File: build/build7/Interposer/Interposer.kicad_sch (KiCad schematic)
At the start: 2 parts, among them U1 BQ21040DBVR, U2 BQ21040DBVR

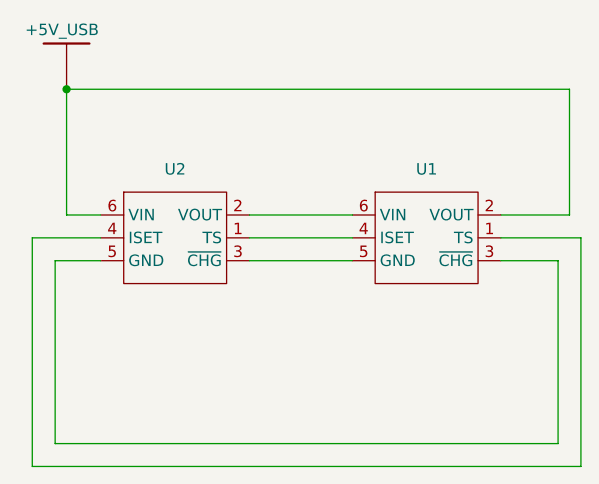
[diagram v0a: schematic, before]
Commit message: Current status: debugged and fixed 4 boards, need to finalize firmware and finish building these 4. All lamps from first build came unglued, need to revise design/assembly to fix this
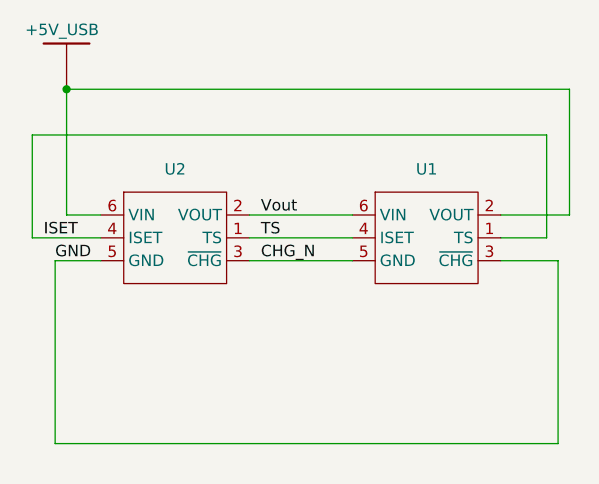
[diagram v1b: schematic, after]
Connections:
- net ISET: now reaches U1.1 (TS), U2.4 (ISET)
- net GND: now reaches U1.3 (~{CHG}), U2.5 (GND)
- net TS: now reaches U1.4 (ISET), U2.1 (TS)
- net CHG_N: now reaches U1.5 (GND), U2.3 (~{CHG})
- net Vout: now reaches U1.6 (VIN), U2.2 (VOUT)
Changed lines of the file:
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@@
-	(wire
-		(pts
-			(xy 161.29 124.46) (xy 161.29 99.06)
-		)
-		(stroke
-			(width 0)
-			(type default)
-		)
-	)
 	(wire
 		(pts
@@
 		(pts
 			(xy 124.46 101.6) (xy 135.89 101.6)
+		)
+		(stroke
+			(width 0)
+			(type default)
+		)
+	)
+	(wire
+		(pts
+			(xy 124.46 99.06) (xy 135.89 99.06)
 		)
 		(stroke
@@
 	(wire
 		(pts
-			(xy 161.29 99.06) (xy 152.4 99.06)
+			(xy 100.33 87.63) (xy 100.33 99.06)
 		)
 		(stroke
@@
 	(wire
 		(pts
+			(xy 157.48 87.63) (xy 157.48 99.06)
+		)
+		(stroke
+			(width 0)
+			(type default)
+		)
+	)
+	(wire
+		(pts
 			(xy 102.87 121.92) (xy 102.87 101.6)
 		)
@@
 	(wire
 		(pts
-			(xy 100.33 124.46) (xy 161.29 124.46)
+			(xy 157.48 99.06) (xy 152.4 99.06)
 		)
 		(stroke
@@
 	(wire
 		(pts
-			(xy 124.46 99.06) (xy 135.89 99.06)
+			(xy 100.33 87.63) (xy 157.48 87.63)
 		)
 		(stroke
@@
 		)
 	)
-	(wire
-		(pts
-			(xy 100.33 99.06) (xy 100.33 124.46)
-		)
-		(stroke
-			(width 0)
-			(type default)
+	(label "GND"
+		(at 102.87 101.6 0)
+		(effects
+			(font
+				(size 1.27 1.27)
+			)
+			(justify left bottom)
 		)
 	)
+	(label "CHG_N"
+		(at 125.73 101.6 0)
+		(effects
+			(font
+				(size 1.27 1.27)
+			)
+			(justify left bottom)
+		)
+	)
+	(label "Vout"
+		(at 125.73 96.52 0)
+		(effects
+			(font
+				(size 1.27 1.27)
+			)
+			(justify left bottom)
+		)
+	)
+	(label "TS"
+		(at 125.73 99.06 0)
+		(effects
+			(font
+				(size 1.27 1.27)
+			)
+			(justify left bottom)
+		)
+	)
+	(label "ISET"
+		(at 101.6 99.06 0)
+		(effects
+			(font
+				(size 1.27 1.27)
+			)
+			(justify left bottom)
+		)
+	)
